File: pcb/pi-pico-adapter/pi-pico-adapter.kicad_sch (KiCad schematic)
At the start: 4 parts, among them J2 RPi_GPIO

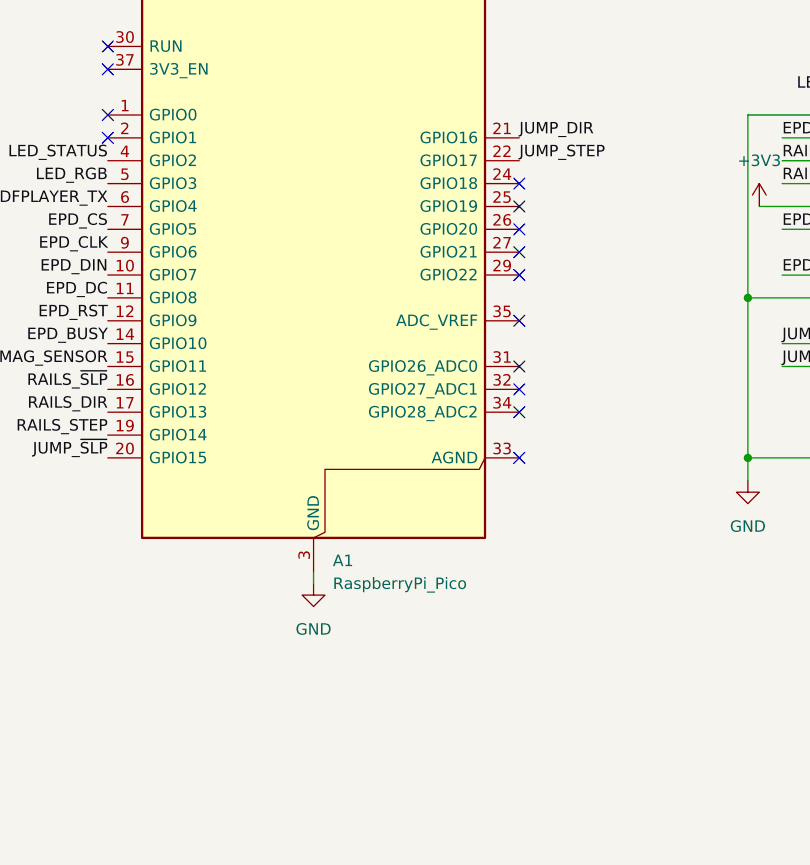
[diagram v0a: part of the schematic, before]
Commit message: feat(pcb): button input (GP18) and mounting holes
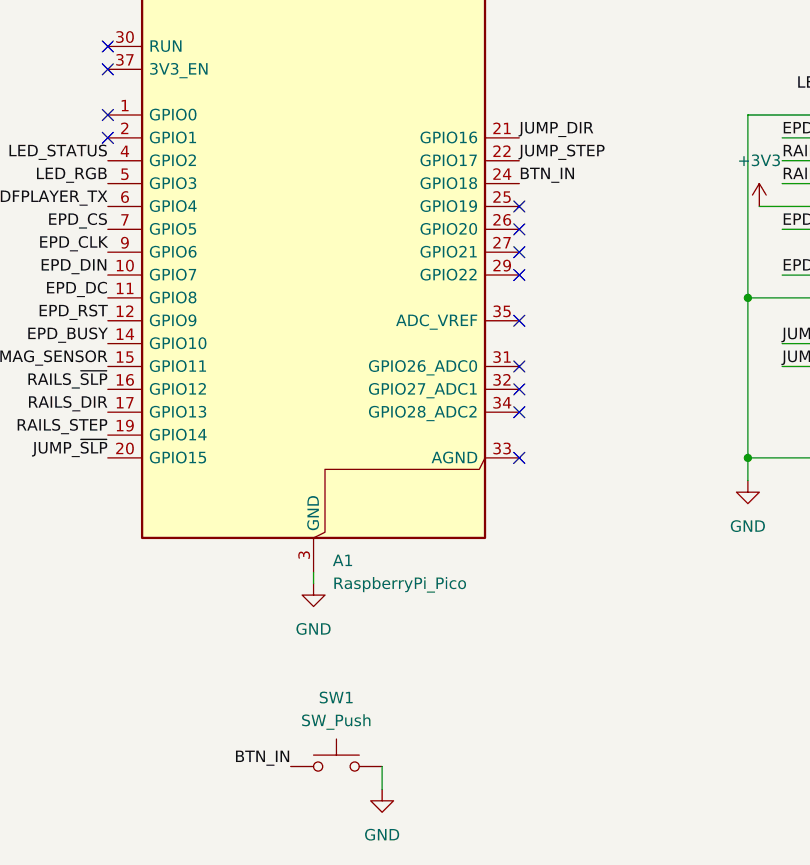
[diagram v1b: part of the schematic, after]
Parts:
- added SW1: SW_Push, Connector_PinHeader_2.54mm:PinHeader_1x02_P2.54mm_Vertical, symbol Switch:SW_Push
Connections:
- net GND: now also SW1.2
- net BTN_IN: now reaches A1.24 (GPIO18)
- net BTN_IN: now also SW1.1
- no-connect marks 27 -> 26
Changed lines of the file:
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@@
-	)
-	(no_connect
-		(at 99.06 102.87)
 	)
 	(no_connect
@@
 	(wire
 		(pts
+			(xy 83.82 167.64) (xy 83.82 170.18)
+		)
+		(stroke
+			(width 0)
+			(type default)
+		)
+	)
+	(wire
+		(pts
 			(xy 191.77 85.09) (xy 195.58 85.09)
 		)
@@
 		)
 	)
+	(label "BTN_IN"
+		(at 73.66 167.64 180)
+		(effects
+			(font
+				(size 1.27 1.27)
+			)
+			(justify right bottom)
+		)
+	)
 	(label "JUMP_~{SLP}"
 		(at 128.27 123.19 0)
+		(effects
+			(font
+				(size 1.27 1.27)
+			)
+			(justify left bottom)
+		)
+	)
+	(label "BTN_IN"
+		(at 99.06 102.87 0)
 		(effects
 			(font
@@
 					(unit 1)
 				)
+			)
+		)
+	)
+	(symbol
+		(lib_id "Switch:SW_Push")
+		(at 78.74 167.64 0)
+		(unit 1)
+		(exclude_from_sim no)
+		(in_bom yes)
+		(on_board yes)
+		(dnp no)
+		(fields_autoplaced yes)
+		(property "Reference" "SW1"
+			(at 78.74 160.02 0)
+			(effects
+				(font
+					(size 1.27 1.27)
+				)
+			)
+		)
+		(property "Value" "SW_Push"
+			(at 78.74 162.56 0)
+			(effects
+				(font
+					(size 1.27 1.27)
+				)
+			)
+		)
+		(property "Footprint" "Connector_PinHeader_2.54mm:PinHeader_1x02_P2.54mm_Vertical"
+			(at 78.74 162.56 0)
+			(effects
+				(font
+					(size 1.27 1.27)
+				)
+				(hide yes)
+			)
+		)
+		(property "Datasheet" "~"
+			(at 78.74 162.56 0)
+			(effects
+				(font
+					(size 1.27 1.27)
+				)
+				(hide yes)
+			)
+		)
+		(property "Description" "Push button switch, generic, two pins"
+			(at 78.74 167.64 0)
+			(effects
+				(font
+					(size 1.27 1.27)
+				)
+				(hide yes)
+			)
+		)
+		(pin "1"
+		)
+		(pin "2"
+		)
+		(instances
+			(project ""
+				(path "/2bb506f1-132a-4112-9134-6a5722b3214e"
+					(reference "SW1")
+					(unit 1)
+				)
+			)
+		)
+	)
+	(symbol
+		(lib_id "power:GND")
+		(at 83.82 170.18 0)
+		(unit 1)
+		(exclude_from_sim no)
+		(in_bom yes)
+		(on_board yes)
+		(dnp no)
+		(fields_autoplaced yes)
+		(property "Reference" "#PWR09"
+			(at 83.82 176.53 0)
+			(effects
+				(font
+					(size 1.27 1.27)
+				)
+				(hide yes)
+			)
+		)
+		(property "Value" "GND"
+			(at 83.82 175.26 0)
+			(effects
+				(font
+					(size 1.27 1.27)
+				)
+			)
+		)
+		(property "Footprint" ""
+			(at 83.82 170.18 0)
+			(effects
+				(font
+					(size 1.27 1.27)
+				)
+				(hide yes)
+			)
+		)
+		(property "Datasheet" ""
+			(at 83.82 170.18 0)
+			(effects
+				(font
+					(size 1.27 1.27)
+				)
+				(hide yes)
+			)
+		)
+		(property "Description" "Power symbol creates a global label with name \"GND\" , ground"
+			(at 83.82 170.18 0)
+			(effects
+				(font
+					(size 1.27 1.27)
+				)
+				(hide yes)
+			)
+		)
+		(pin "1"
+		)
+		(instances
+			(project "pi-pico-adapter"
+				(path "/2bb506f1-132a-4112-9134-6a5722b3214e"
+					(reference "#PWR09")
+					(unit 1)
+				)
